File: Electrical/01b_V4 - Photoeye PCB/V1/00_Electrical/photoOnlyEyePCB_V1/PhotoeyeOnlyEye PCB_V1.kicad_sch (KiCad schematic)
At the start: 4 parts, among them J1 B3B-PH-SM4-TB(LF)(SN), U2 RPR-220

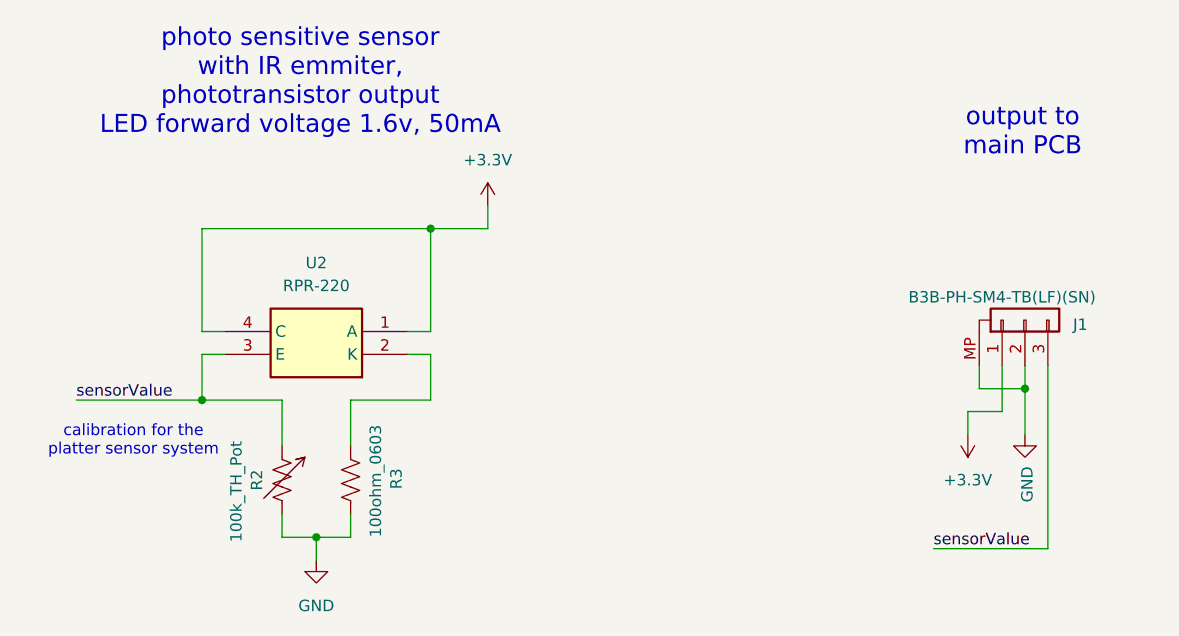
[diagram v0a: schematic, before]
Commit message: fixing the crossed wire for the photo sensor. deleting the old CNC jobs. Re-exporting gerbers and schematics. Re-mill with new files
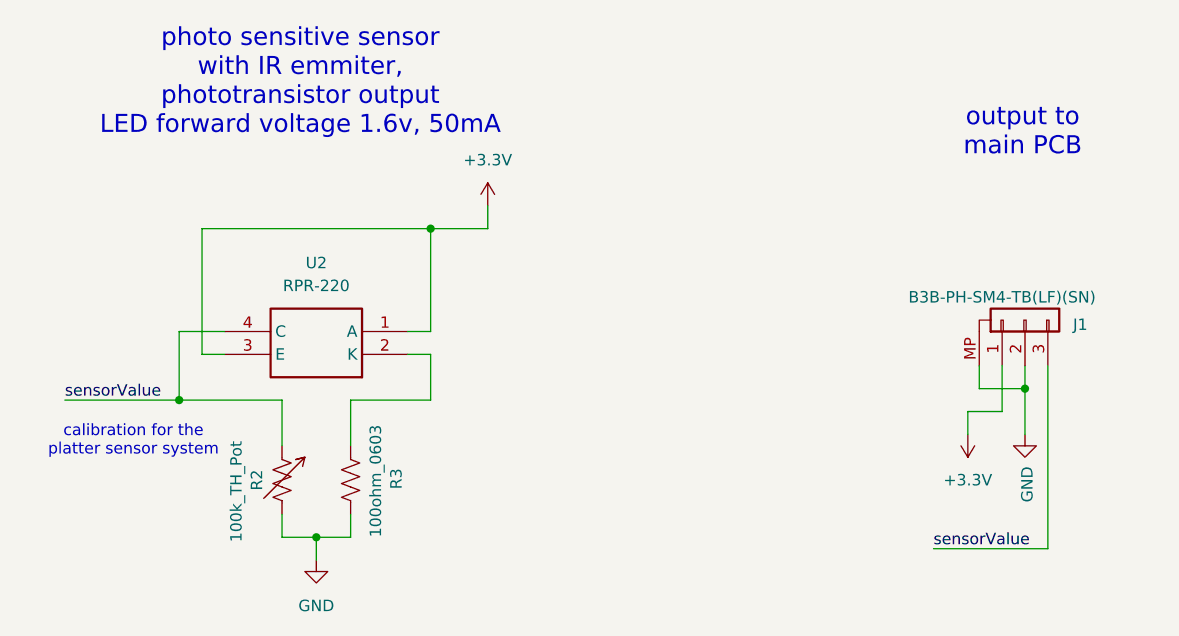
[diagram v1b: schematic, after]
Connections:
- net +3.3V: now also U2.3 (E); no longer U2.4 (C)
- net sensorValue: now also U2.4 (C); no longer U2.3 (E)
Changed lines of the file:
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@@
 	)
 	(junction
-		(at 92.71 86.36)
+		(at 90.17 86.36)
 		(diameter 0)
 		(color 0 0 0 0)
@@
 	(wire
 		(pts
-			(xy 92.71 86.36) (xy 101.6 86.36)
-		)
-		(stroke
-			(width 0)
-			(type default)
-		)
-	)
-	(wire
-		(pts
 			(xy 177.8 87.63) (xy 181.61 87.63)
 		)
@@
 	(wire
 		(pts
+			(xy 90.17 86.36) (xy 101.6 86.36)
+		)
+		(stroke
+			(width 0)
+			(type default)
+		)
+	)
+	(wire
+		(pts
 			(xy 118.11 78.74) (xy 118.11 67.31)
 		)
@@
 	(wire
 		(pts
+			(xy 95.25 78.74) (xy 90.17 78.74)
+		)
+		(stroke
+			(width 0)
+			(type default)
+		)
+	)
+	(wire
+		(pts
 			(xy 184.15 85.09) (xy 184.15 90.17)
 		)
@@
 	(wire
 		(pts
-			(xy 92.71 78.74) (xy 92.71 67.31)
+			(xy 92.71 67.31) (xy 92.71 81.28)
 		)
 		(stroke
@@
 	(wire
 		(pts
-			(xy 95.25 81.28) (xy 92.71 81.28)
+			(xy 92.71 81.28) (xy 95.25 81.28)
 		)
 		(stroke
@@
 	(wire
 		(pts
-			(xy 78.74 86.36) (xy 92.71 86.36)
-		)
-		(stroke
-			(width 0)
-			(type default)
-		)
-	)
-	(wire
-		(pts
-			(xy 92.71 81.28) (xy 92.71 86.36)
+			(xy 77.47 86.36) (xy 90.17 86.36)
+		)
+		(stroke
+			(width 0)
+			(type default)
+		)
+	)
+	(wire
+		(pts
+			(xy 90.17 78.74) (xy 90.17 86.36)
 		)
 		(stroke
@@
 		(pts
 			(xy 173.99 102.87) (xy 186.69 102.87)
-		)
-		(stroke
-			(width 0)
-			(type default)
-		)
-	)
-	(wire
-		(pts
-			(xy 95.25 78.74) (xy 92.71 78.74)
 		)
 		(stroke
@@
 	)
 	(label "sensorValue"
-		(at 78.74 86.36 0)
+		(at 77.47 86.36 0)
 		(effects
 			(font
